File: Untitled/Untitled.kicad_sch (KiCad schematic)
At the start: 8 parts

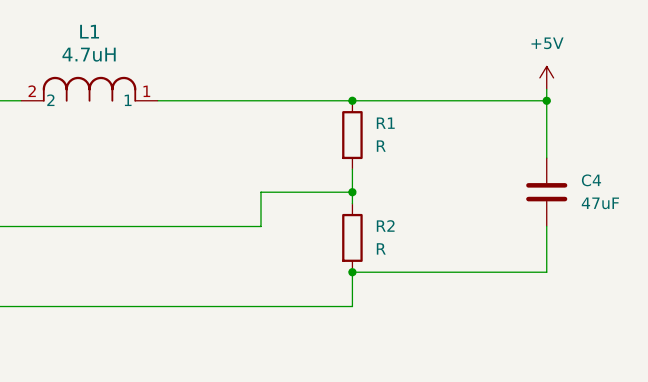
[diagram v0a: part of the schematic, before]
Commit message: added r values
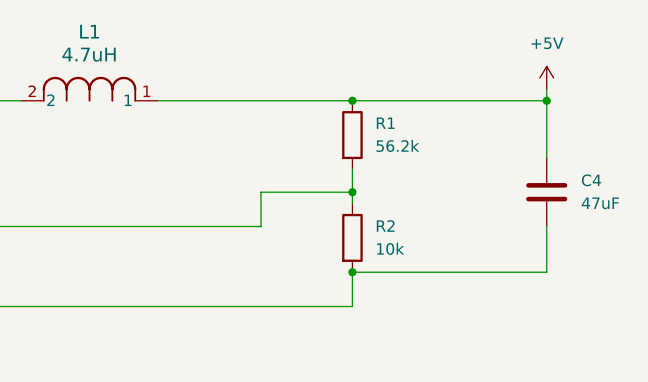
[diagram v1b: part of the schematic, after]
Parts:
- R1: value R -> 56.2k
- R2: value R -> 10k
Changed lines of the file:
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@@
 			)
 		)
-		(property "Value" "R"
+		(property "Value" "56.2k"
 			(at 209.55 66.0399 0)
 			(effects
@@
 			)
 		)
-		(property "Value" "R"
+		(property "Value" "10k"
 			(at 209.55 77.4699 0)
 			(effects

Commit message: created pcb and imported all footprints
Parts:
- L1: footprint IND_EPCOS_B82462A4_EPC -> drum:IND_EPCOS_B82462A4_EPC
- VR1: footprint (none) -> ic:SOT95P280X110-6N
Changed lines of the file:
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@@
 			)
 		)
-		(property "Footprint" ""
+		(property "Footprint" "ic:SOT95P280X110-6N"
 			(at 133.35 71.12 0)
 			(effects
@@
 			)
 		)
-		(property "Footprint" "IND_EPCOS_B82462A4_EPC"
+		(property "Footprint" "drum:IND_EPCOS_B82462A4_EPC"
 			(at 170.18 60.96 0)
 			(effects

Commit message: updated TP footprint and added names
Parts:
- added 12v_in: 12v_in, TestPoint:TestPoint_Plated_Hole_D2.0mm, symbol Connector:TestPoint
- added GND_in: GND_in, TestPoint:TestPoint_Plated_Hole_D2.0mm, symbol Connector:TestPoint
- added TP3: vout_1, TestPoint:TestPoint_Plated_Hole_D2.0mm, symbol Connector:TestPoint
- added TP4: vout_2, TestPoint:TestPoint_Plated_Hole_D2.0mm, symbol Connector:TestPoint
- added g_out1: g_out1, TestPoint:TestPoint_Plated_Hole_D2.0mm, symbol Connector:TestPoint
- added g_out2: g_out2, TestPoint:TestPoint_Plated_Hole_D2.0mm, symbol Connector:TestPoint
- added g_out3: g_out3, TestPoint:TestPoint_Plated_Hole_D2.0mm, symbol Connector:TestPoint
- added vout_3: vout_3, TestPoint:TestPoint_Plated_Hole_D2.0mm, symbol Connector:TestPoint
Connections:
- net +12V: now also 12v_in.1
- net +5V: now also TP3.1, TP4.1, vout_3.1
- net GND: now also GND_in.1, g_out1.1, g_out2.1, g_out3.1

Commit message: version1
I wanna figure out how to reduce the size somehow. but this version should work fine
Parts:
- 12v_in1: renamed from 12v_in; footprint TestPoint:TestPoint_Plated_Hole_D2.0mm -> TestPoint:TestPoint_Pad_D2.5mm
- GND_in1: renamed from GND_in; footprint TestPoint:TestPoint_Plated_Hole_D2.0mm -> TestPoint:TestPoint_Pad_D2.5mm
- renumbered TP3 to v_out1, TP4 to v_out2
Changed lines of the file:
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@@
 				)
 				(justify left)
+				(hide yes)
 			)
 		)
@@
 				)
 				(justify left)
+				(hide yes)
 			)
 		)
@@
 		(dnp no)
 		(fields_autoplaced yes)
-		(property "Reference" "TP3"
-			(at 233.68 53.3399 90)
+		(property "Reference" "v_out1"
+			(at 233.68 54.6099 90)
 			(effects
 				(font
@@
 				)
 				(justify left)
+				(hide yes)
 			)
 		)
@@
 			(project "Untitled"
 				(path "/f79f3f11-fb75-40ce-b012-bbf43826134e"
-					(reference "TP3")
+					(reference "v_out1")
 					(unit 1)
 				)
@@
 				)
 				(justify left)
+				(hide yes)
 			)
 		)
@@
 		(dnp no)
 		(fields_autoplaced yes)
-		(property "Reference" "TP4"
-			(at 233.68 48.2599 90)
+		(property "Reference" "v_out2"
+			(at 233.68 49.5299 90)
 			(effects
 				(font
@@
 				)
 				(justify left)
+				(hide yes)
 			)
 		)
@@
 			(project "Untitled"
 				(path "/f79f3f11-fb75-40ce-b012-bbf43826134e"
-					(reference "TP4")
+					(reference "v_out2")
 					(unit 1)
 				)
@@
 				)
 				(justify left)
+				(hide yes)
 			)
 		)
@@
 		(dnp no)
 		(fields_autoplaced yes)
-		(property "Reference" "12v_in"
+		(property "Reference" "12v_in1"
 			(at 83.82 52.5779 0)
 			(effects
@@
 				)
 				(justify left)
-			)
-		)
-		(property "Footprint" "TestPoint:TestPoint_Plated_Hole_D2.0mm"
+				(hide yes)
+			)
+		)
+		(property "Footprint" "TestPoint:TestPoint_Pad_D2.5mm"
 			(at 86.36 57.15 0)
 			(effects
@@
 			(project ""
 				(path "/f79f3f11-fb75-40ce-b012-bbf43826134e"
-					(reference "12v_in")
+					(reference "12v_in1")
 					(unit 1)
 				)
@@
 		(dnp no)
 		(fields_autoplaced yes)
-		(property "Reference" "GND_in"
+		(property "Reference" "GND_in1"
 			(at 83.82 90.9319 0)
 			(effects
@@
 				)
 				(justify right)
-			)
-		)
-		(property "Footprint" "TestPoint:TestPoint_Plated_Hole_D2.0mm"
+				(hide yes)
+			)
+		)
+		(property "Footprint" "TestPoint:TestPoint_Pad_D2.5mm"
 			(at 76.2 88.9 0)
 			(effects
@@
 			(project "Untitled"
 				(path "/f79f3f11-fb75-40ce-b012-bbf43826134e"
-					(reference "GND_in")
-					(unit 1)
-				)
+					(reference "GND_in1")
+					(unit 1)
+				)

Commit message: updated to 2.54tht pads
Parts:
- C4: footprint Capacitor_SMD:C_0603_1608Metric_Pad1.08x0.95mm_HandSolder -> Capacitor_SMD:C_1206_3216Metric_Pad1.33x1.80mm_HandSolder
- g_out1, g_out2, g_out3, v_out1, v_out2, vout_3: footprint TestPoint:TestPoint_Plated_Hole_D2.0mm -> Connector_PinHeader_2.54mm:PinHeader_1x01_P2.54mm_Vertical
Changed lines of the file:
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@@
 			)
 		)
-		(property "Footprint" "TestPoint:TestPoint_Plated_Hole_D2.0mm"
+		(property "Footprint" "Connector_PinHeader_2.54mm:PinHeader_1x01_P2.54mm_Vertical"
 			(at 228.6 85.09 0)
 			(effects
@@
 			)
 		)
-		(property "Footprint" "TestPoint:TestPoint_Plated_Hole_D2.0mm"
+		(property "Footprint" "Connector_PinHeader_2.54mm:PinHeader_1x01_P2.54mm_Vertical"
 			(at 228.6 90.17 0)
 			(effects
@@
 			)
 		)
-		(property "Footprint" "TestPoint:TestPoint_Plated_Hole_D2.0mm"
+		(property "Footprint" "Connector_PinHeader_2.54mm:PinHeader_1x01_P2.54mm_Vertical"
 			(at 228.6 59.69 0)
 			(effects
@@
 			)
 		)
-		(property "Footprint" "Capacitor_SMD:C_0603_1608Metric_Pad1.08x0.95mm_HandSolder"
+		(property "Footprint" "Capacitor_SMD:C_1206_3216Metric_Pad1.33x1.80mm_HandSolder"
 			(at 227.6348 67.31 0)
 			(effects
@@
 			)
 		)
-		(property "Footprint" "TestPoint:TestPoint_Plated_Hole_D2.0mm"
+		(property "Footprint" "Connector_PinHeader_2.54mm:PinHeader_1x01_P2.54mm_Vertical"
 			(at 228.6 95.25 0)
 			(effects
@@
 			)
 		)
-		(property "Footprint" "TestPoint:TestPoint_Plated_Hole_D2.0mm"
+		(property "Footprint" "Connector_PinHeader_2.54mm:PinHeader_1x01_P2.54mm_Vertical"
 			(at 228.6 54.61 0)
 			(effects
@@
 			)
 		)
-		(property "Footprint" "TestPoint:TestPoint_Plated_Hole_D2.0mm"
+		(property "Footprint" "Connector_PinHeader_2.54mm:PinHeader_1x01_P2.54mm_Vertical"
 			(at 228.6 49.53 0)
 			(effects
